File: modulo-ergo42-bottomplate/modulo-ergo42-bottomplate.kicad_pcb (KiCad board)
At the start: 2 copper layers, 137.2 x 80 mm, 14 parts

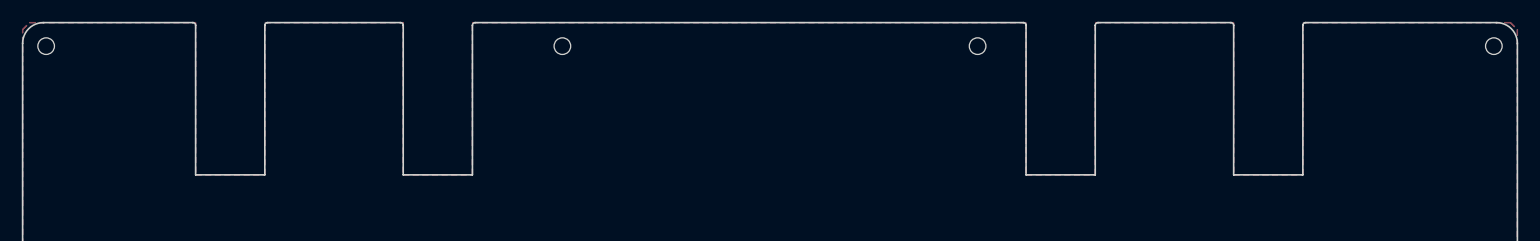
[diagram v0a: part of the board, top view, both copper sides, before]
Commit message: Add DIP switch window
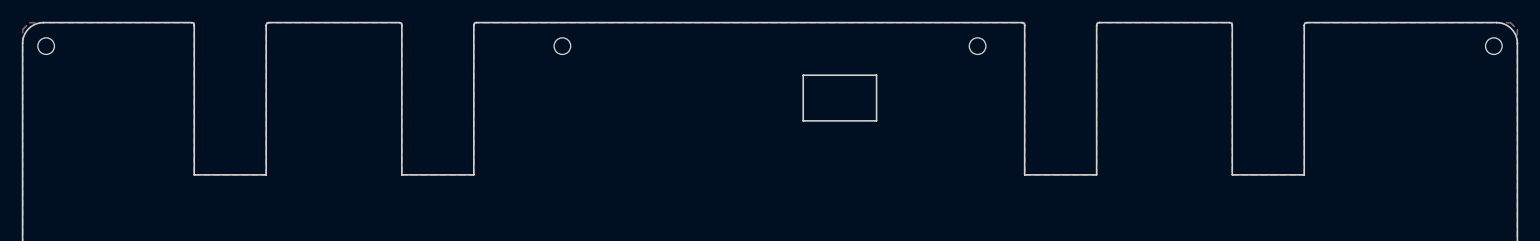
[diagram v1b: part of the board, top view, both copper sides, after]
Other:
- outline, holes or cut-outs redrawn
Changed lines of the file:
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@@
   (general
     (thickness 1.6)
-    (drawings 32)
+    (drawings 36)
     (tracks 0)
     (zones 0)
@@
     (pad "" np_thru_hole circle (at 0 0) (size 1.524 1.524) (drill 1.524) (layers *.Cu *.Mask))
   )
-  (gr_arc (start 146.431 34.544) (end 146.685 34.544) (angle -90) (layer Edge.Cuts) (width 0.15))
-  (gr_arc (start 153.289 34.544) (end 153.289 34.29) (angle -90) (layer Edge.Cuts) (width 0.15))
-  (gr_line (start 146.685 48.26) (end 153.035 48.26) (layer Edge.Cuts) (width 0.15))
-  (gr_line (start 153.035 34.544) (end 153.035 48.26) (layer Edge.Cuts) (width 0.15))
-  (gr_line (start 146.685 34.544) (end 146.685 48.26) (layer Edge.Cuts) (width 0.15))
-  (gr_line (start 153.289 34.29) (end 165.481 34.29) (layer Edge.Cuts) (width 0.15))
-  (gr_arc (start 165.481 34.544) (end 165.735 34.544) (angle -90) (layer Edge.Cuts) (width 0.15))
-  (gr_arc (start 172.339 34.544) (end 172.339 34.29) (angle -90) (layer Edge.Cuts) (width 0.15))
-  (gr_line (start 165.735 48.26) (end 172.085 48.26) (layer Edge.Cuts) (width 0.15))
-  (gr_line (start 172.085 34.544) (end 172.085 48.26) (layer Edge.Cuts) (width 0.15))
-  (gr_line (start 165.735 34.544) (end 165.735 48.26) (layer Edge.Cuts) (width 0.15))
-  (gr_line (start 172.339 34.29) (end 189.865 34.29) (layer Edge.Cuts) (width 0.15))
-  (gr_arc (start 89.281 34.544) (end 89.535 34.544) (angle -90) (layer Edge.Cuts) (width 0.15))
-  (gr_arc (start 96.139 34.544) (end 96.139 34.29) (angle -90) (layer Edge.Cuts) (width 0.15))
-  (gr_line (start 95.885 48.26) (end 89.535 48.26) (layer Edge.Cuts) (width 0.15))
-  (gr_line (start 95.885 34.544) (end 95.885 48.26) (layer Edge.Cuts) (width 0.15))
-  (gr_line (start 96.139 34.29) (end 146.431 34.29) (layer Edge.Cuts) (width 0.15))
-  (gr_line (start 89.535 34.544) (end 89.535 48.26) (layer Edge.Cuts) (width 0.15))
-  (gr_arc (start 77.089 34.544) (end 77.089 34.29) (angle -90) (layer Edge.Cuts) (width 0.15))
-  (gr_arc (start 70.231 34.544) (end 70.485 34.544) (angle -90) (layer Edge.Cuts) (width 0.15))
-  (gr_line (start 70.485 34.544) (end 70.485 48.26) (layer Edge.Cuts) (width 0.15))
-  (gr_line (start 76.835 34.544) (end 76.835 48.26) (layer Edge.Cuts) (width 0.15))
-  (gr_line (start 70.485 48.26) (end 76.835 48.26) (layer Edge.Cuts) (width 0.15))
-  (gr_line (start 77.089 34.29) (end 89.281 34.29) (layer Edge.Cuts) (width 0.15))
+  (gr_line (start 126.238 43.307) (end 126.238 39.116) (layer Edge.Cuts) (width 0.15))
+  (gr_line (start 132.969 43.307) (end 126.238 43.307) (layer Edge.Cuts) (width 0.15))
+  (gr_line (start 132.969 39.116) (end 132.969 43.307) (layer Edge.Cuts) (width 0.15))
+  (gr_line (start 126.238 39.116) (end 132.969 39.116) (layer Edge.Cuts) (width 0.15))
+  (gr_arc (start 146.304 34.544) (end 146.558 34.544) (angle -90) (layer Edge.Cuts) (width 0.15))
+  (gr_arc (start 153.416 34.544) (end 153.416 34.29) (angle -90) (layer Edge.Cuts) (width 0.15))
+  (gr_line (start 146.558 48.26) (end 153.162 48.26) (layer Edge.Cuts) (width 0.15))
+  (gr_line (start 153.162 34.544) (end 153.162 48.26) (layer Edge.Cuts) (width 0.15))
+  (gr_line (start 146.558 34.544) (end 146.558 48.26) (layer Edge.Cuts) (width 0.15))
+  (gr_line (start 153.416 34.29) (end 165.354 34.29) (layer Edge.Cuts) (width 0.15))
+  (gr_arc (start 165.354 34.544) (end 165.608 34.544) (angle -90) (layer Edge.Cuts) (width 0.15))
+  (gr_arc (start 172.466 34.544) (end 172.466 34.29) (angle -90) (layer Edge.Cuts) (width 0.15))
+  (gr_line (start 165.608 48.26) (end 172.212 48.26) (layer Edge.Cuts) (width 0.15))
+  (gr_line (start 172.212 34.544) (end 172.212 48.26) (layer Edge.Cuts) (width 0.15))
+  (gr_line (start 165.608 34.544) (end 165.608 48.26) (layer Edge.Cuts) (width 0.15))
+  (gr_line (start 172.466 34.29) (end 189.865 34.29) (layer Edge.Cuts) (width 0.15))
+  (gr_arc (start 89.154 34.544) (end 89.408 34.544) (angle -90) (layer Edge.Cuts) (width 0.15))
+  (gr_arc (start 96.266 34.544) (end 96.266 34.29) (angle -90) (layer Edge.Cuts) (width 0.15))
+  (gr_line (start 96.012 48.26) (end 89.408 48.26) (layer Edge.Cuts) (width 0.15))
+  (gr_line (start 96.012 34.544) (end 96.012 48.26) (layer Edge.Cuts) (width 0.15))
+  (gr_line (start 96.266 34.29) (end 146.304 34.29) (layer Edge.Cuts) (width 0.15))
+  (gr_line (start 89.408 34.544) (end 89.408 48.26) (layer Edge.Cuts) (width 0.15))
+  (gr_arc (start 77.216 34.544) (end 77.216 34.29) (angle -90) (layer Edge.Cuts) (width 0.15))
+  (gr_arc (start 70.104 34.544) (end 70.358 34.544) (angle -90) (layer Edge.Cuts) (width 0.15))
+  (gr_line (start 70.358 34.544) (end 70.358 48.26) (layer Edge.Cuts) (width 0.15))
+  (gr_line (start 76.962 34.544) (end 76.962 48.26) (layer Edge.Cuts) (width 0.15))
+  (gr_line (start 70.358 48.26) (end 76.962 48.26) (layer Edge.Cuts) (width 0.15))
+  (gr_line (start 77.216 34.29) (end 89.154 34.29) (layer Edge.Cuts) (width 0.15))
   (gr_arc (start 56.515 112.395) (end 54.61 112.395) (angle -90) (layer Edge.Cuts) (width 0.15))
   (gr_arc (start 189.865 112.395) (end 189.865 114.3) (angle -90) (layer Edge.Cuts) (width 0.15))
@@
   (gr_line (start 54.61 36.195) (end 54.61 112.395) (layer Edge.Cuts) (width 0.15))
   (gr_line (start 191.77 36.195) (end 191.77 112.395) (layer Edge.Cuts) (width 0.15))
-  (gr_line (start 56.515 34.29) (end 70.231 34.29) (layer Edge.Cuts) (width 0.15))
+  (gr_line (start 56.515 34.29) (end 70.104 34.29) (layer Edge.Cuts) (width 0.15))
   (zone (net 0) (net_name "") (layer B.Cu) (hatch edge 0.508)
     (connect_pads (clearance 0.508))
@@
     (polygon
       (pts
-        (xy 70.485 34.29) (xy 70.485 48.26) (xy 76.835 48.26) (xy 76.835 34.29) (xy 89.535 34.29)
-        (xy 89.535 48.26) (xy 95.885 48.26) (xy 95.885 34.29) (xy 146.685 34.29) (xy 146.685 48.26)
-        (xy 153.035 48.26) (xy 153.035 34.29) (xy 165.735 34.29) (xy 165.735 48.26) (xy 172.085 48.26)
-        (xy 172.085 34.29) (xy 191.135 34.29) (xy 191.77 34.925) (xy 191.77 113.665) (xy 191.135 114.3)
+        (xy 70.358 34.29) (xy 70.358 48.26) (xy 76.962 48.26) (xy 76.962 34.29) (xy 89.408 34.29)
+        (xy 89.408 48.26) (xy 96.012 48.26) (xy 96.012 34.29) (xy 146.558 34.29) (xy 146.558 48.26)
+        (xy 153.162 48.26) (xy 153.162 34.29) (xy 165.608 34.29) (xy 165.608 48.26) (xy 172.212 48.26)
+        (xy 172.212 34.29) (xy 191.135 34.29) (xy 191.77 34.925) (xy 191.77 113.665) (xy 191.135 114.3)
         (xy 55.245 114.3) (xy 54.61 113.665) (xy 54.61 34.925) (xy 55.245 34.29)
       )
@@
     (polygon
       (pts
-        (xy 70.485 34.29) (xy 70.485 48.26) (xy 76.835 48.26) (xy 76.835 34.29) (xy 89.535 34.29)
-        (xy 89.535 48.26) (xy 95.885 48.26) (xy 95.885 34.29) (xy 146.685 34.29) (xy 146.685 48.26)
-        (xy 153.035 48.26) (xy 153.035 34.29) (xy 165.735 34.29) (xy 165.735 48.26) (xy 172.085 48.26)
-        (xy 172.085 34.29) (xy 191.135 34.29) (xy 191.77 34.925) (xy 191.77 113.665) (xy 191.135 114.3)
+        (xy 70.358 34.29) (xy 70.358 48.26) (xy 76.962 48.26) (xy 76.962 34.29) (xy 89.408 34.29)
+        (xy 89.408 48.26) (xy 96.012 48.26) (xy 96.012 34.29) (xy 146.558 34.29) (xy 146.558 48.26)
+        (xy 153.162 48.26) (xy 153.162 34.29) (xy 165.608 34.29) (xy 165.608 48.26) (xy 172.212 48.26)
+        (xy 172.212 34.29) (xy 191.135 34.29) (xy 191.77 34.925) (xy 191.77 113.665) (xy 191.135 114.3)
         (xy 55.245 114.3) (xy 54.61 113.665) (xy 54.61 34.925) (xy 55.245 34.29)
       )
     )
+  )
+  (zone (net 0) (net_name "") (layers F&B.Cu) (hatch edge 0.508)
+    (connect_pads (clearance 0.508))
+    (min_thickness 0.254)
+    (keepout (tracks not_allowed) (vias not_allowed) (copperpour not_allowed))
+    (fill (arc_segments 16) (thermal_gap 0.508) (thermal_bridge_width 0.508))
+    (polygon
+      (pts
+        (xy 126.238 39.116) (xy 126.238 43.307) (xy 132.969 43.307) (xy 132.969 39.116)
+      )
+    )

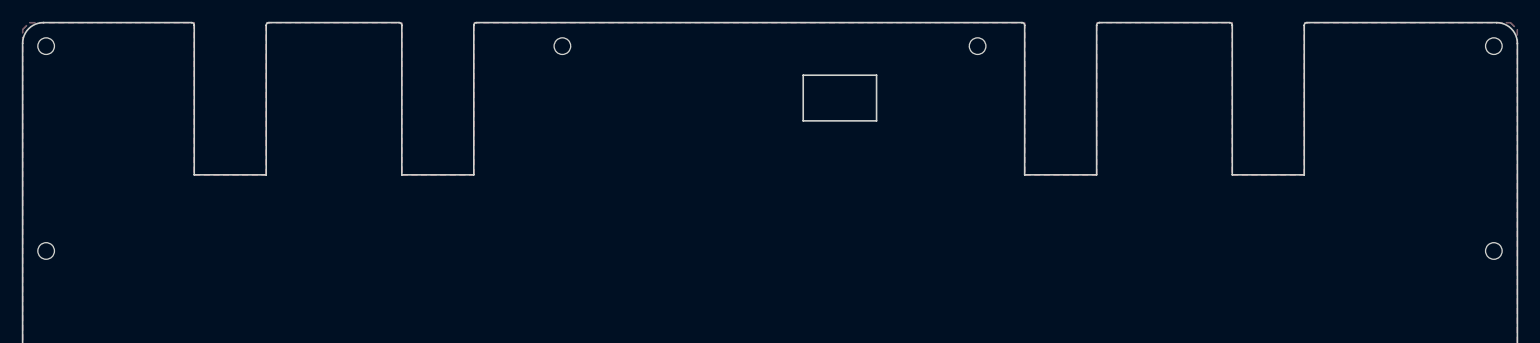
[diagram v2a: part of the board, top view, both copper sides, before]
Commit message: Update bottom plate for Beta-1
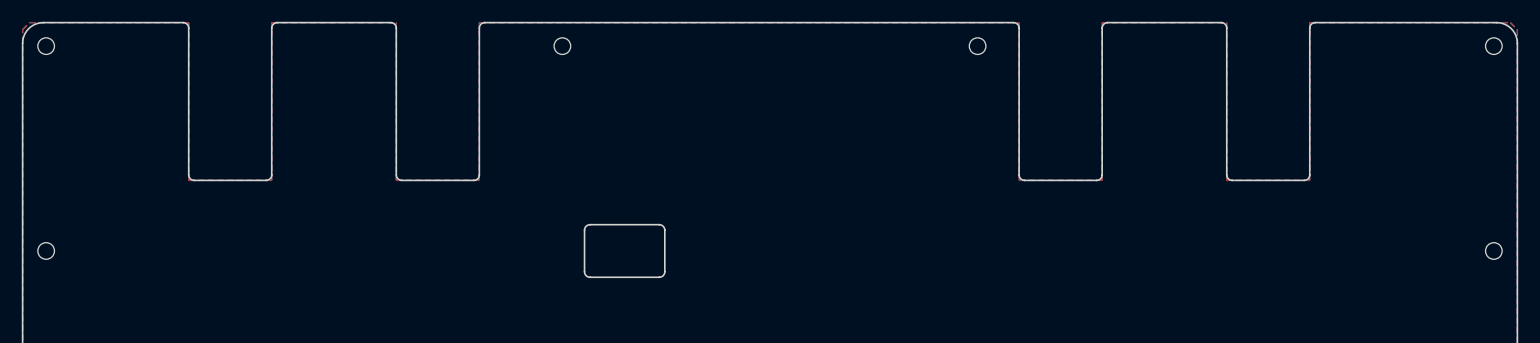
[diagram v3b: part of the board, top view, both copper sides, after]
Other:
- outline, holes or cut-outs redrawn
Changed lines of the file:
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@@
-(kicad_pcb (version 20171130) (host pcbnew 5.0.1-33cea8e~68~ubuntu18.04.1)
+(kicad_pcb (version 20171130) (host pcbnew 5.0.2-bee76a0~70~ubuntu18.04.1)
   (general
     (thickness 1.6)
-    (drawings 36)
+    (drawings 48)
     (tracks 0)
     (zones 0)
@@
     (pad "" np_thru_hole circle (at 0 0) (size 1.524 1.524) (drill 1.524) (layers *.Cu *.Mask))
   )
-  (gr_line (start 126.238 43.307) (end 126.238 39.116) (layer Edge.Cuts) (width 0.15))
-  (gr_line (start 132.969 43.307) (end 126.238 43.307) (layer Edge.Cuts) (width 0.15))
-  (gr_line (start 132.969 39.116) (end 132.969 43.307) (layer Edge.Cuts) (width 0.15))
-  (gr_line (start 126.238 39.116) (end 132.969 39.116) (layer Edge.Cuts) (width 0.15))
-  (gr_arc (start 146.304 34.544) (end 146.558 34.544) (angle -90) (layer Edge.Cuts) (width 0.15))
-  (gr_arc (start 153.416 34.544) (end 153.416 34.29) (angle -90) (layer Edge.Cuts) (width 0.15))
-  (gr_line (start 146.558 48.26) (end 153.162 48.26) (layer Edge.Cuts) (width 0.15))
-  (gr_line (start 153.162 34.544) (end 153.162 48.26) (layer Edge.Cuts) (width 0.15))
-  (gr_line (start 146.558 34.544) (end 146.558 48.26) (layer Edge.Cuts) (width 0.15))
-  (gr_line (start 153.416 34.29) (end 165.354 34.29) (layer Edge.Cuts) (width 0.15))
-  (gr_arc (start 165.354 34.544) (end 165.608 34.544) (angle -90) (layer Edge.Cuts) (width 0.15))
-  (gr_arc (start 172.466 34.544) (end 172.466 34.29) (angle -90) (layer Edge.Cuts) (width 0.15))
-  (gr_line (start 165.608 48.26) (end 172.212 48.26) (layer Edge.Cuts) (width 0.15))
-  (gr_line (start 172.212 34.544) (end 172.212 48.26) (layer Edge.Cuts) (width 0.15))
-  (gr_line (start 165.608 34.544) (end 165.608 48.26) (layer Edge.Cuts) (width 0.15))
-  (gr_line (start 172.466 34.29) (end 189.865 34.29) (layer Edge.Cuts) (width 0.15))
-  (gr_arc (start 89.154 34.544) (end 89.408 34.544) (angle -90) (layer Edge.Cuts) (width 0.15))
-  (gr_arc (start 96.266 34.544) (end 96.266 34.29) (angle -90) (layer Edge.Cuts) (width 0.15))
-  (gr_line (start 96.012 48.26) (end 89.408 48.26) (layer Edge.Cuts) (width 0.15))
-  (gr_line (start 96.012 34.544) (end 96.012 48.26) (layer Edge.Cuts) (width 0.15))
-  (gr_line (start 96.266 34.29) (end 146.304 34.29) (layer Edge.Cuts) (width 0.15))
-  (gr_line (start 89.408 34.544) (end 89.408 48.26) (layer Edge.Cuts) (width 0.15))
-  (gr_arc (start 77.216 34.544) (end 77.216 34.29) (angle -90) (layer Edge.Cuts) (width 0.15))
-  (gr_arc (start 70.104 34.544) (end 70.358 34.544) (angle -90) (layer Edge.Cuts) (width 0.15))
-  (gr_line (start 70.358 34.544) (end 70.358 48.26) (layer Edge.Cuts) (width 0.15))
-  (gr_line (start 76.962 34.544) (end 76.962 48.26) (layer Edge.Cuts) (width 0.15))
-  (gr_line (start 70.358 48.26) (end 76.962 48.26) (layer Edge.Cuts) (width 0.15))
-  (gr_line (start 77.216 34.29) (end 89.154 34.29) (layer Edge.Cuts) (width 0.15))
+  (gr_arc (start 113.03 57.15) (end 113.03 57.658) (angle -90) (layer Edge.Cuts) (width 0.15))
+  (gr_arc (start 106.68 57.15) (end 106.172 57.15) (angle -90) (layer Edge.Cuts) (width 0.15))
+  (gr_arc (start 106.68 53.34) (end 106.68 52.832) (angle -90) (layer Edge.Cuts) (width 0.15))
+  (gr_arc (start 113.03 53.34) (end 113.538 53.34) (angle -90) (layer Edge.Cuts) (width 0.15))
+  (gr_line (start 106.172 53.34) (end 106.172 57.15) (layer Edge.Cuts) (width 0.15))
+  (gr_line (start 113.03 57.658) (end 106.68 57.658) (layer Edge.Cuts) (width 0.15))
+  (gr_line (start 113.538 53.34) (end 113.538 57.15) (layer Edge.Cuts) (width 0.15))
+  (gr_line (start 106.68 52.832) (end 113.03 52.832) (layer Edge.Cuts) (width 0.15))
+  (gr_arc (start 165.608 48.26) (end 165.1 48.26) (angle -90) (layer Edge.Cuts) (width 0.15))
+  (gr_arc (start 172.212 48.26) (end 172.212 48.768) (angle -90) (layer Edge.Cuts) (width 0.15))
+  (gr_arc (start 146.558 48.26) (end 146.05 48.26) (angle -90) (layer Edge.Cuts) (width 0.15))
+  (gr_arc (start 153.162 48.26) (end 153.162 48.768) (angle -90) (layer Edge.Cuts) (width 0.15))
+  (gr_arc (start 154.178 34.798) (end 154.178 34.29) (angle -90) (layer Edge.Cuts) (width 0.15))
+  (gr_arc (start 145.542 34.798) (end 146.05 34.798) (angle -90) (layer Edge.Cuts) (width 0.15))
+  (gr_arc (start 89.408 48.26) (end 88.9 48.26) (angle -90) (layer Edge.Cuts) (width 0.15))
+  (gr_arc (start 96.012 48.26) (end 96.012 48.768) (angle -90) (layer Edge.Cuts) (width 0.15))
+  (gr_arc (start 88.392 34.798) (end 88.9 34.798) (angle -90) (layer Edge.Cuts) (width 0.15))
+  (gr_arc (start 97.028 34.798) (end 97.028 34.29) (angle -90) (layer Edge.Cuts) (width 0.15))
+  (gr_arc (start 69.342 34.798) (end 69.85 34.798) (angle -90) (layer Edge.Cuts) (width 0.15))
+  (gr_arc (start 70.358 48.26) (end 69.85 48.26) (angle -90) (layer Edge.Cuts) (width 0.15))
+  (gr_arc (start 76.962 48.26) (end 76.962 48.768) (angle -90) (layer Edge.Cuts) (width 0.15))
+  (gr_arc (start 77.978 34.798) (end 77.978 34.29) (angle -90) (layer Edge.Cuts) (width 0.15))
+  (gr_line (start 146.558 48.768) (end 153.162 48.768) (layer Edge.Cuts) (width 0.15))
+  (gr_line (start 153.67 34.798) (end 153.67 48.26) (layer Edge.Cuts) (width 0.15))
+  (gr_line (start 146.05 34.798) (end 146.05 48.26) (layer Edge.Cuts) (width 0.15))
+  (gr_line (start 154.178 34.29) (end 164.592 34.29) (layer Edge.Cuts) (width 0.15))
+  (gr_arc (start 164.592 34.798) (end 165.1 34.798) (angle -90) (layer Edge.Cuts) (width 0.15))
+  (gr_arc (start 173.228 34.798) (end 173.228 34.29) (angle -90) (layer Edge.Cuts) (width 0.15))
+  (gr_line (start 165.608 48.768) (end 172.212 48.768) (layer Edge.Cuts) (width 0.15))
+  (gr_line (start 172.72 34.798) (end 172.72 48.26) (layer Edge.Cuts) (width 0.15))
+  (gr_line (start 165.1 34.798) (end 165.1 48.26) (layer Edge.Cuts) (width 0.15))
+  (gr_line (start 173.228 34.29) (end 189.865 34.29) (layer Edge.Cuts) (width 0.15))
+  (gr_line (start 96.012 48.768) (end 89.408 48.768) (layer Edge.Cuts) (width 0.15))
+  (gr_line (start 96.52 34.798) (end 96.52 48.26) (layer Edge.Cuts) (width 0.15))
+  (gr_line (start 97.028 34.29) (end 145.542 34.29) (layer Edge.Cuts) (width 0.15))
+  (gr_line (start 88.9 34.798) (end 88.9 48.26) (layer Edge.Cuts) (width 0.15))
+  (gr_line (start 69.85 34.798) (end 69.85 48.26) (layer Edge.Cuts) (width 0.15))
+  (gr_line (start 77.47 34.798) (end 77.47 48.26) (layer Edge.Cuts) (width 0.15))
+  (gr_line (start 70.358 48.768) (end 76.962 48.768) (layer Edge.Cuts) (width 0.15))
+  (gr_line (start 77.978 34.29) (end 88.392 34.29) (layer Edge.Cuts) (width 0.15))
   (gr_arc (start 56.515 112.395) (end 54.61 112.395) (angle -90) (layer Edge.Cuts) (width 0.15))
   (gr_arc (start 189.865 112.395) (end 189.865 114.3) (angle -90) (layer Edge.Cuts) (width 0.15))
@@
   (gr_line (start 54.61 36.195) (end 54.61 112.395) (layer Edge.Cuts) (width 0.15))
   (gr_line (start 191.77 36.195) (end 191.77 112.395) (layer Edge.Cuts) (width 0.15))
-  (gr_line (start 56.515 34.29) (end 70.104 34.29) (layer Edge.Cuts) (width 0.15))
+  (gr_line (start 56.515 34.29) (end 69.342 34.29) (layer Edge.Cuts) (width 0.15))
   (zone (net 0) (net_name "") (layer B.Cu) (hatch edge 0.508)
     (connect_pads (clearance 0.508))
@@
     (polygon
       (pts
-        (xy 70.358 34.29) (xy 70.358 48.26) (xy 76.962 48.26) (xy 76.962 34.29) (xy 89.408 34.29)
-        (xy 89.408 48.26) (xy 96.012 48.26) (xy 96.012 34.29) (xy 146.558 34.29) (xy 146.558 48.26)
-        (xy 153.162 48.26) (xy 153.162 34.29) (xy 165.608 34.29) (xy 165.608 48.26) (xy 172.212 48.26)
-        (xy 172.212 34.29) (xy 191.135 34.29) (xy 191.77 34.925) (xy 191.77 113.665) (xy 191.135 114.3)
+        (xy 69.85 34.29) (xy 69.85 48.768) (xy 77.47 48.768) (xy 77.47 34.29) (xy 88.9 34.29)
+        (xy 88.9 48.768) (xy 96.52 48.768) (xy 96.52 34.29) (xy 146.05 34.29) (xy 146.05 48.768)
+        (xy 153.67 48.768) (xy 153.67 34.29) (xy 165.1 34.29) (xy 165.1 48.768) (xy 172.72 48.768)
+        (xy 172.72 34.29) (xy 191.135 34.29) (xy 191.77 34.925) (xy 191.77 113.665) (xy 191.135 114.3)
         (xy 55.245 114.3) (xy 54.61 113.665) (xy 54.61 34.925) (xy 55.245 34.29)
       )
@@
     (polygon
       (pts
-        (xy 70.358 34.29) (xy 70.358 48.26) (xy 76.962 48.26) (xy 76.962 34.29) (xy 89.408 34.29)
-        (xy 89.408 48.26) (xy 96.012 48.26) (xy 96.012 34.29) (xy 146.558 34.29) (xy 146.558 48.26)
-        (xy 153.162 48.26) (xy 153.162 34.29) (xy 165.608 34.29) (xy 165.608 48.26) (xy 172.212 48.26)
-        (xy 172.212 34.29) (xy 191.135 34.29) (xy 191.77 34.925) (xy 191.77 113.665) (xy 191.135 114.3)
+        (xy 69.85 34.29) (xy 69.85 48.768) (xy 77.47 48.768) (xy 77.47 34.29) (xy 88.9 34.29)
+        (xy 88.9 48.768) (xy 96.52 48.768) (xy 96.52 34.29) (xy 146.05 34.29) (xy 146.05 48.768)
+        (xy 153.67 48.768) (xy 153.67 34.29) (xy 165.1 34.29) (xy 165.1 48.768) (xy 172.72 48.768)
+        (xy 172.72 34.29) (xy 191.135 34.29) (xy 191.77 34.925) (xy 191.77 113.665) (xy 191.135 114.3)
         (xy 55.245 114.3) (xy 54.61 113.665) (xy 54.61 34.925) (xy 55.245 34.29)
       )
@@
     (polygon
       (pts
-        (xy 126.238 39.116) (xy 126.238 43.307) (xy 132.969 43.307) (xy 132.969 39.116)
+        (xy 106.172 52.832) (xy 113.538 52.832) (xy 113.538 57.658) (xy 106.172 57.658)
       )
     )
